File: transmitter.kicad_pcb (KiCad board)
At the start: 2 copper layers, 265 parts, among them J1 JST PHD B12B, J10 HR911105A, J2 JST PHD B12B, J3 JST PHD B12B, J4 JST PHD B12B, J5 JST PHD B12B, J6 JST PHD B12B, J7 JST PHD B12B, J8 JST PH B4B, J9 DC Barrel Jack, U1 STM32H723ZGT, U10 AM26LV32E, U11 SRV05-4, U12 SRV05-4, U13 AM26LV32E, U14 SRV05-4, U15 SRV05-4, U16 AM26LV32E, U17 SRV05-4, U18 SRV05-4, U19 AM26LV32E, U2 LMR33630B, U20 SRV05-4, U21 SRV05-4, U22 AM26LV32E, U23 SRV05-4, U24 SRV05-4, U25 AM26LV32E, U26 SRV05-4, U27 SRV05-4, U28 AM26LV32E, U29 SRV05-4, U3 TLV76733, U30 SRV05-4, U31 AM26LV32E, U4 LAN8742AI, U5 SRV05-4, U6 SRV05-4, U7 AM26LV32E, U8 SRV05-4, U9 SRV05-4, Y1 ABM8G-25MHz

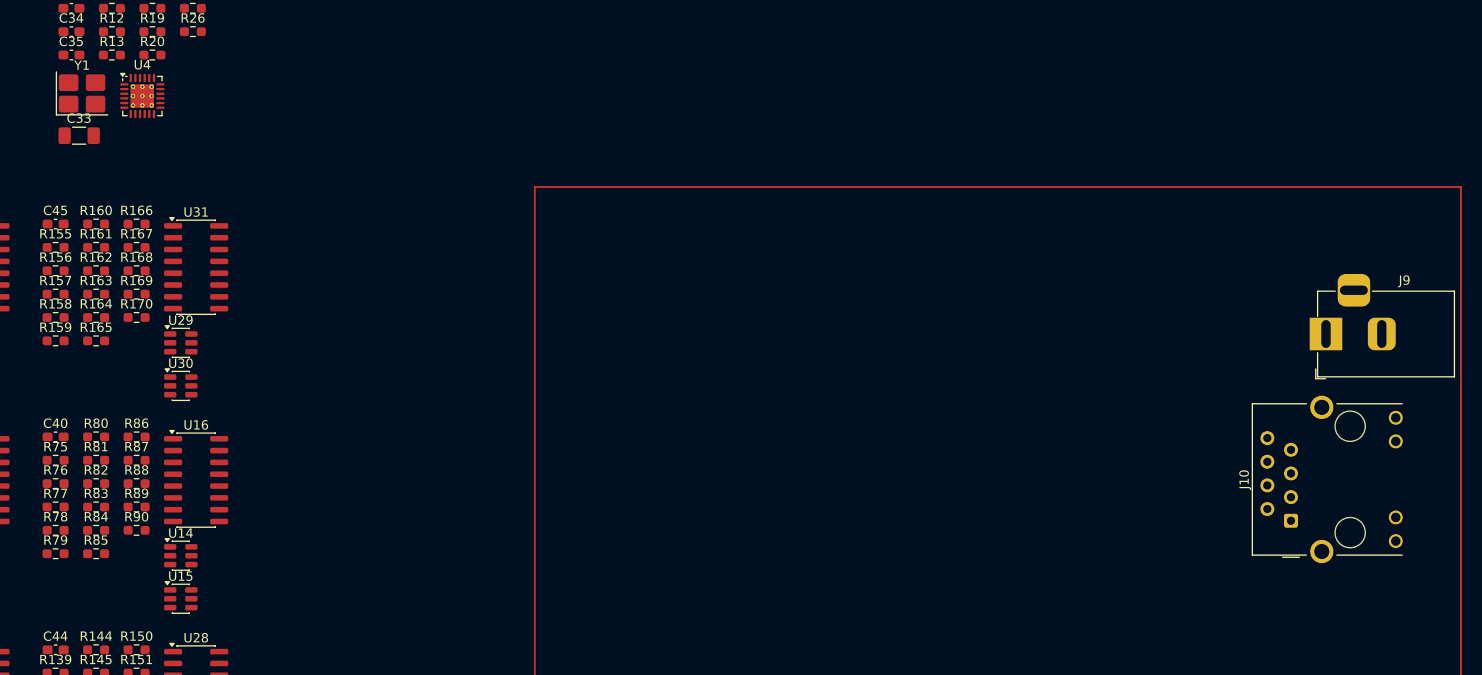
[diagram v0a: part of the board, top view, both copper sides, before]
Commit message: Updated power connector
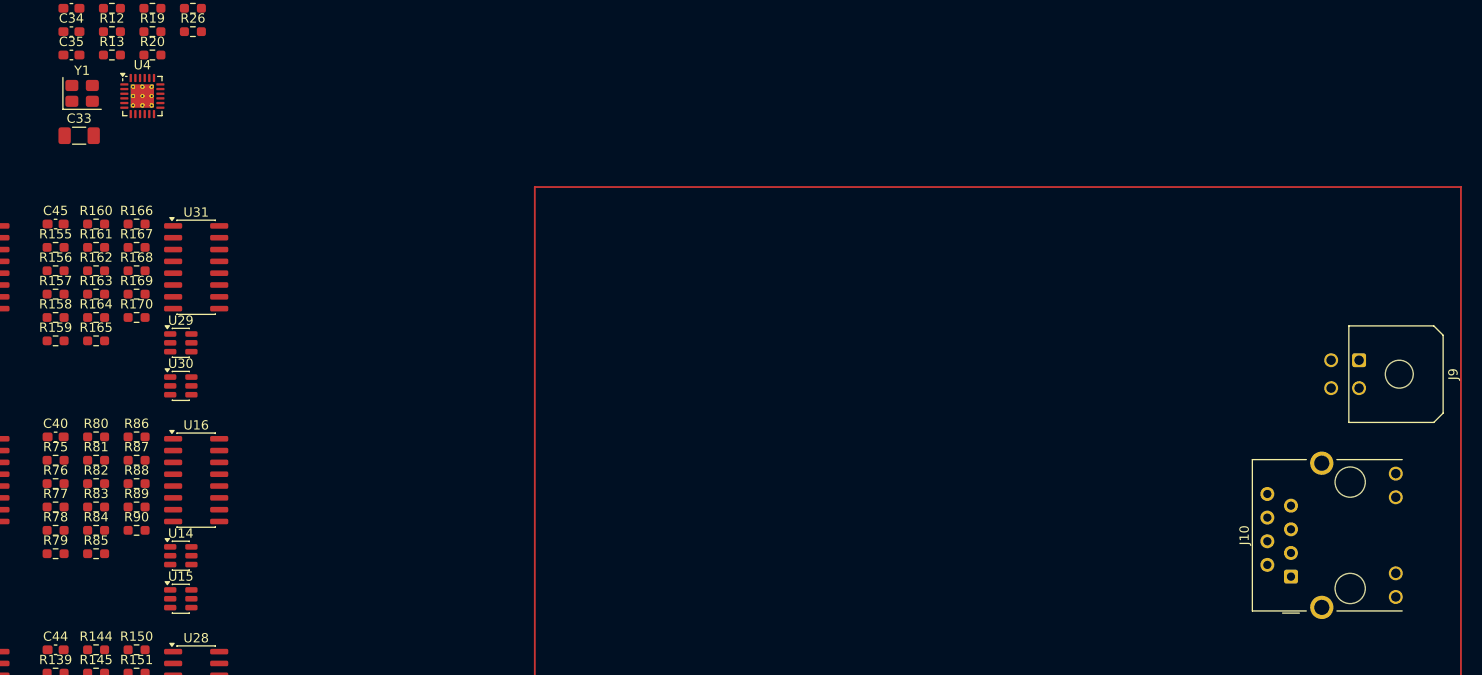
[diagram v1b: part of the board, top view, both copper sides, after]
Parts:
- J9: value DC Barrel Jack -> Power MX 3.0; footprint Connector_BarrelJack:BarrelJack_Horizontal -> Connector_Molex:Molex_Micro-Fit_3.0_43045-0400_2x02_P3.00mm_Horizontal
- Y1: footprint Crystal:Crystal_SMD_3225-4Pin_3.2x2.5mm_HandSoldering -> Crystal:Crystal_SMD_3225-4Pin_3.2x2.5mm
- moved J10 6.00 mm to (231.7, 91.9)
- moved J9 4.53 mm to (239.1, 68.6), turned to -90 degrees
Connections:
- J9 pad 2: GND -> VDD
- J9 pad 3: (no net) -> GND
